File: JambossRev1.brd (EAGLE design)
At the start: 81.3 x 38.1 mm, 29 parts, among them CN1 1X4-BIG, CN2 1X4-BIG, J1 AVR_SPI_PRG_6NS, Q1 16MhZ, U1 MCP73831, U2 ATMEGA328P

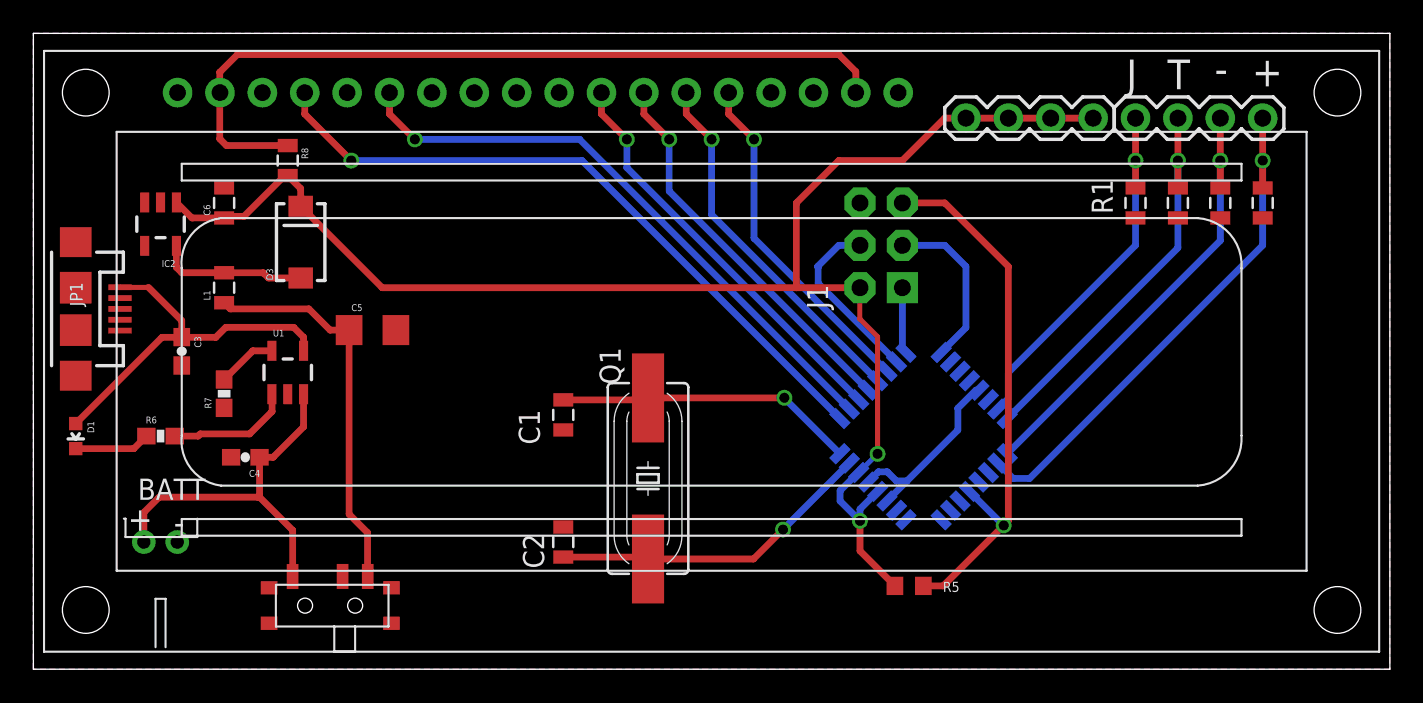
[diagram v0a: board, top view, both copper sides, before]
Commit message: Board Layout
Improved silk readability
Moved the LCD resistor to the proper place
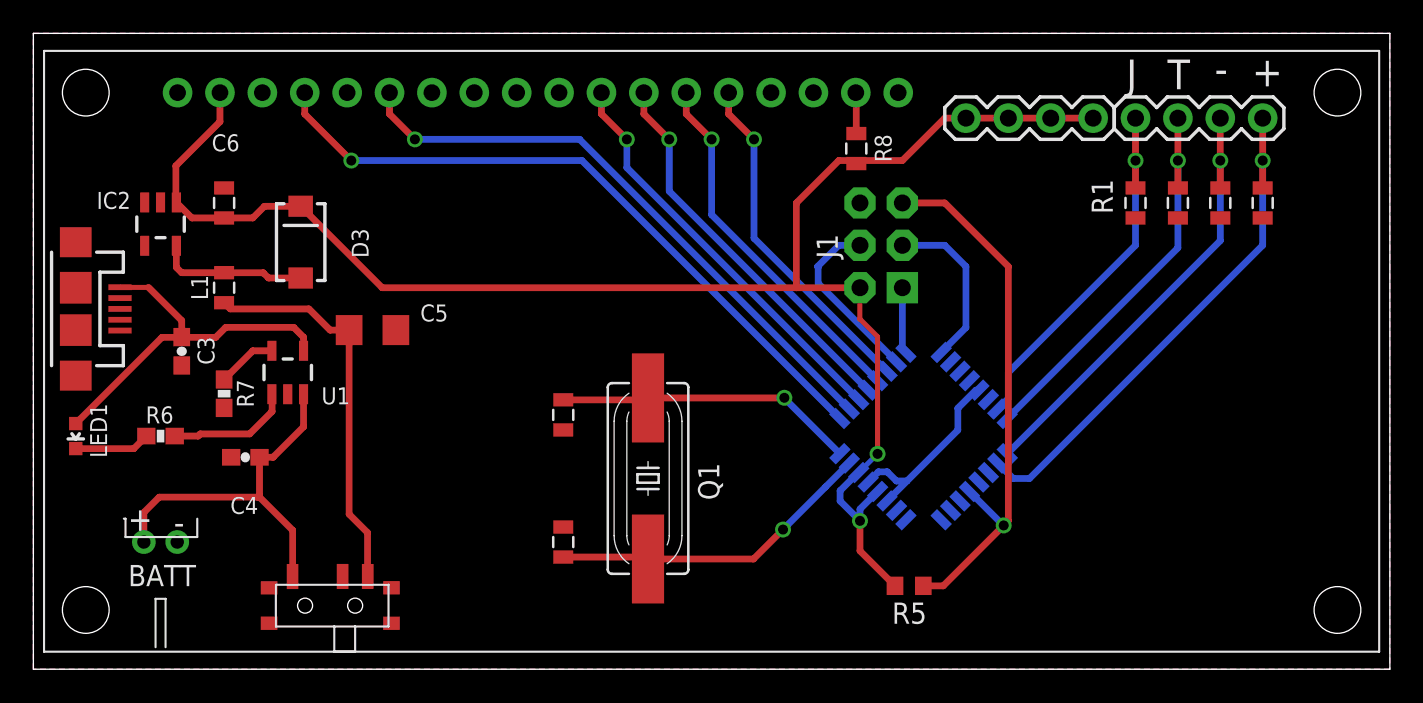
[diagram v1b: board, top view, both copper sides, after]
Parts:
- IC2: value (none) -> NCP1402
- R7: value 2.0k -> 2k
- moved R8 34.1 mm to (49.3, 31.2)
- renumbered D1 to LED1
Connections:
- removed net VDD: R8.1, U$2.17, U$2.2
- new net GRN: R8.1, U$2.17
- net VCC: now also U$2.2
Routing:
- net VDD: track 48.5 -> 0.00 mm
- net VCC: track 93.6 -> 99.1 mm
- net GRN: track 0.00 -> 2.46 mm

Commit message: Switch, silkscreen, xtal
Fixed on/off switch connections
Swapped xtal for identical with smaller footprint, shorter profile
(saved 3 cents)
Arranged silk labels for easier reading
Added OSH logo and github URL to bottom silk
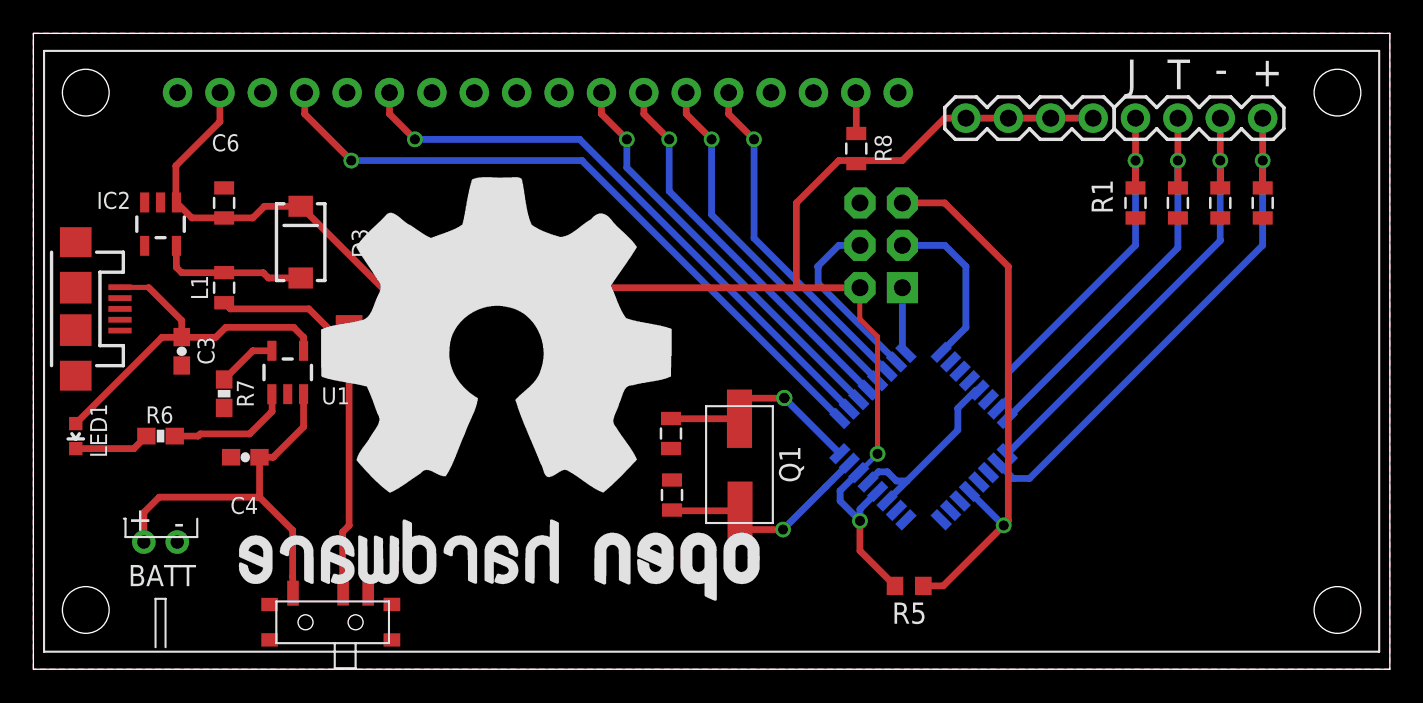
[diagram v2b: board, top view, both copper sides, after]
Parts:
- Q1: value 16MhZ -> 70X41SMDXTAL; device SparkFun-FreqCtrl:HC49UP -> iconcustom:XTAL-70X41
- U$3: device SparkFun-Aesthetics:OSHW-LOGO-L -> iconcustom:OSH-LOGO-HUGE
- moved U$3 43.0 mm to (27.8, 19.0)
- moved C2 7.10 mm to (38.3, 10.4)
- moved C1 6.55 mm to (38.2, 14.1)
- moved Q1 5.54 mm to (42.3, 12.3)
- moved U$1 1.00 mm to (17.8, 2.81)
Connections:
- net N$1: now also Q1.P$1; no longer Q1.2
- net N$2: now also Q1.P$2; no longer Q1.1
- net N$22: now also U$1.2; no longer U$1.3
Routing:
- net N$1: track 19.6 -> 13.4 mm
- net N$2: track 18.0 -> 12.8 mm, vias 1 -> 2
- net V_BATT: track 22.5 -> 23.4 mm
- net N$22: track 23.4 -> 24.1 mm
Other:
- board text added: "https://github.com/andricongirl/JamBoss"
